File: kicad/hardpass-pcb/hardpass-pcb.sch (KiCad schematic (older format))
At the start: 54 parts, among them P1 Pi_Zero, P2 OLED_I2C, SW1 1, SW10 C/UP, SW11 0/OK, SW12 OK/DN, SW13 SHUTDN, SW2 2, SW3 3, SW4 4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

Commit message: created footprint for sim slot
will use a linkconn sim connector, available from aliexpress using the term 'samsung note n7000 i9000 9003 sim connector'
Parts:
- C? (x14): footprint (none) -> Capacitors_SMD:C_1206
- R? (x2): footprint (none) -> Resistors_SMD:R_1206
- U?: footprint (none) -> Housings_QFP:LQFP-32_7x7mm_Pitch0.8mm
- U?: footprint (none) -> hardpass:CAF99-08153-S132
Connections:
- net +3V3: no longer C?.1, C?.1, C?.2, C?.2, SW?.1, U?.1 (P17), U?.10 (K2), U?.16 (DCIN), U?.21 (EA_N), U?.3 (VDD)
- new net +5V: C?.1, C?.1, C?.2, C?.2, SW?.1, U?.1 (P17), U?.10 (K2), U?.16 (DCIN), U?.21 (EA_N), U?.3 (VDD)
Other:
- note added: "Sim card socket: 'samsung n7000 i9003' style\nhttp://www.linkconn.com/en/product/e08f128a-897a-4361-86f3-81b7a41ba7d4"
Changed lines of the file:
@@
 F 0 "C?" H 10510 3220 50  0000 L CNN
 F 1 "220nF" H 10510 3070 50  0000 L CNN
-F 2 "" H 10500 3150 50  0000 C CNN
+F 2 "Capacitors_SMD:C_1206" H 10600 4850 50  0001 C CNN
 F 3 "" H 10500 3150 50  0000 C CNN
 	1    10500 3150
@@
 F 0 "C?" H 10760 3220 50  0000 L CNN
 F 1 "220nF" H 10760 3070 50  0000 L CNN
-F 2 "" H 10750 3150 50  0000 C CNN
+F 2 "Capacitors_SMD:C_1206" H 10600 4750 50  0001 C CNN
 F 3 "" H 10750 3150 50  0000 C CNN
 	1    10750 3150
@@
 F 0 "C?" H 10110 3870 50  0000 L CNN
 F 1 "100nF" V 10000 3650 50  0000 L CNN
-F 2 "" H 10100 3800 50  0000 C CNN
+F 2 "Capacitors_SMD:C_1206" H 10100 3800 50  0001 C CNN
 F 3 "" H 10100 3800 50  0000 C CNN
 	1    10100 3800
@@
 F 0 "C?" H 10110 4070 50  0000 L CNN
 F 1 "10µF" V 10200 3850 50  0000 L CNN
-F 2 "" H 10100 4000 50  0000 C CNN
+F 2 "Capacitors_SMD:C_1206" H 10100 4000 50  0001 C CNN
 F 3 "" H 10100 4000 50  0000 C CNN
 	1    10100 4000
@@
 F 0 "C?" H 9710 3670 50  0000 L CNN
 F 1 "220nF" H 9710 3520 50  0000 L CNN
-F 2 "" H 9700 3600 50  0000 C CNN
+F 2 "Capacitors_SMD:C_1206" H 9700 3600 50  0001 C CNN
 F 3 "" H 9700 3600 50  0000 C CNN
 	1    9700 3600
@@
 F 0 "C?" H 8360 3670 50  0000 L CNN
 F 1 "100pF" H 8360 3520 50  0000 L CNN
-F 2 "" H 8350 3600 50  0000 C CNN
+F 2 "Capacitors_SMD:C_1206" H 8350 3600 50  0001 C CNN
 F 3 "" H 8350 3600 50  0000 C CNN
 	1    8350 3600
@@
 F 0 "C?" H 7660 3470 50  0000 L CNN
 F 1 "220nF" H 7660 3320 50  0000 L CNN
-F 2 "" H 7650 3400 50  0000 C CNN
+F 2 "Capacitors_SMD:C_1206" H 7650 3400 50  0001 C CNN
 F 3 "" H 7650 3400 50  0000 C CNN
 	1    7650 3400
@@
 F 0 "C?" V 8750 2750 50  0000 L CNN
 F 1 "22nF" V 8750 2450 50  0000 L CNN
-F 2 "" H 8700 2700 50  0000 C CNN
+F 2 "Capacitors_SMD:C_1206" V 7350 4600 50  0001 C CNN
 F 3 "" H 8700 2700 50  0000 C CNN
 	1    8700 2700
@@
 F 0 "C?" H 8460 2270 50  0000 L CNN
 F 1 "100nF" V 8350 2100 50  0000 L CNN
-F 2 "" H 8450 2200 50  0000 C CNN
+F 2 "Capacitors_SMD:C_1206" V 9400 50  50  0001 C CNN
 F 3 "" H 8450 2200 50  0000 C CNN
 	1    8450 2200
@@
 F 0 "C?" H 8460 2020 50  0000 L CNN
 F 1 "10µF" V 8350 1850 50  0000 L CNN
-F 2 "" H 8450 1950 50  0000 C CNN
+F 2 "Capacitors_SMD:C_1206" V 9250 -200 50  0001 C CNN
 F 3 "" H 8450 1950 50  0000 C CNN
 	1    8450 1950
@@
 $EndComp
 $Comp
-L +3V3 #PWR?
-U 1 1 5880FFCE
-P 8600 1950
-F 0 "#PWR?" H 8600 1800 50  0001 C CNN
-F 1 "+3V3" H 8600 2090 50  0001 C CNN
-F 2 "" H 8600 1950 50  0000 C CNN
-F 3 "" H 8600 1950 50  0000 C CNN
-	1    8600 1950
-	1    0    0    -1
-$EndComp
-$Comp
-L +3V3 #PWR?
-U 1 1 588135B2
-P 10650 2500
-F 0 "#PWR?" H 10650 2350 50  0001 C CNN
-F 1 "+3V3" H 10650 2640 50  0000 C CNN
-F 2 "" H 10650 2500 50  0000 C CNN
-F 3 "" H 10650 2500 50  0000 C CNN
-	1    10650 2500
-	1    0    0    -1
-$EndComp
-$Comp
 L GND #PWR?
 U 1 1 5881377E
@@
 F 0 "U?" H 7050 3550 60  0000 C CNN
 F 1 "ISO7816" H 7050 2750 60  0000 C CNN
-F 2 "" H 7050 3250 60  0001 C CNN
+F 2 "hardpass:CAF99-08153-S132" H 7050 3250 60  0001 C CNN
 F 3 "" H 7050 3250 60  0001 C CNN
 	1    7050 3150
 	1    0    0    1
-$EndComp
-$Comp
-L +3V3 #PWR?
-U 1 1 58821E3C
-P 7550 2900
-F 0 "#PWR?" H 7550 2750 50  0001 C CNN
-F 1 "+3V3" H 7550 3040 50  0001 C CNN
-F 2 "" H 7550 2900 50  0000 C CNN
-F 3 "" H 7550 2900 50  0000 C CNN
-	1    7550 2900
-	1    0    0    -1
 $EndComp
 NoConn ~ 7450 3100
@@
 F 0 "R?" H 8230 2820 50  0000 L CNN
 F 1 "180" H 8230 2760 50  0000 L CNN
-F 2 "" H 8200 2800 50  0000 C CNN
+F 2 "Resistors_SMD:R_1206" H 8200 2800 50  0001 C CNN
 F 3 "" H 8200 2800 50  0000 C CNN
 	1    8200 2800
@@
 F 0 "C?" H 8060 3270 50  0000 L CNN
 F 1 "33pF" H 8060 3120 50  0000 L CNN
-F 2 "" H 8050 3200 50  0000 C CNN
+F 2 "Capacitors_SMD:C_1206" H 8050 3200 50  0001 C CNN
 F 3 "" H 8050 3200 50  0000 C CNN
 	1    8050 3200
@@
 F 0 "C?" H 8860 3670 50  0000 L CNN
 F 1 "100pF" H 8860 3520 50  0000 L CNN
-F 2 "" H 8850 3600 50  0000 C CNN
+F 2 "Capacitors_SMD:C_1206" H 8850 3600 50  0001 C CNN
 F 3 "" H 8850 3600 50  0000 C CNN
 	1    8850 3600
@@
 	1    0    0    -1
 $EndComp
-$Comp
-L +3V3 #PWR?
-U 1 1 58833391
-P 10200 3400
-F 0 "#PWR?" H 10200 3250 50  0001 C CNN
-F 1 "+3V3" H 10200 3540 50  0000 C CNN
-F 2 "" H 10200 3400 50  0000 C CNN
-F 3 "" H 10200 3400 50  0000 C CNN
-	1    10200 3400
-	1    0    0    -1
-$EndComp
 Text Notes 6450 4300 0    60   ~ 0
 http://www.nxp.com/documents/application_note/AN10207.pdf\nhttp://www.nxp.com/documents/data_sheet/TDA8029.pdf
@@
 F 0 "C?" H 10010 1270 50  0000 L CNN
 F 1 "22pF" H 10010 1120 50  0000 L CNN
-F 2 "" H 10000 1200 50  0000 C CNN
+F 2 "Capacitors_SMD:C_1206" H 10600 1350 50  0001 C CNN
 F 3 "" H 10000 1200 50  0000 C CNN
 	1    10000 1200
@@
 F 0 "C?" H 9710 1270 50  0000 L CNN
 F 1 "22pF" H 9710 1120 50  0000 L CNN
-F 2 "" H 9700 1200 50  0000 C CNN
+F 2 "Capacitors_SMD:C_1206" H 8800 1450 50  0001 C CNN
 F 3 "" H 9700 1200 50  0000 C CNN
 	1    9700 1200
@@
 $EndComp
 $Comp
-L +3V3 #PWR?
-U 1 1 58840082
-P 9500 1500
-F 0 "#PWR?" H 9500 1350 50  0001 C CNN
-F 1 "+3V3" H 9500 1640 50  0001 C CNN
-F 2 "" H 9500 1500 50  0000 C CNN
-F 3 "" H 9500 1500 50  0000 C CNN
-	1    9500 1500
-	1    0    0    -1
-$EndComp
-$Comp
-L +3V3 #PWR?
-U 1 1 58843822
-P 8800 2200
-F 0 "#PWR?" H 8800 2050 50  0001 C CNN
-F 1 "+3V3" H 8800 2340 50  0001 C CNN
-F 2 "" H 8800 2200 50  0000 C CNN
-F 3 "" H 8800 2200 50  0000 C CNN
-	1    8800 2200
-	1    0    0    -1
-$EndComp
-$Comp
 L TDA8029 U?
 U 1 1 5880AAA0
@@
 F 0 "U?" H 9650 2450 60  0000 C CNN
 F 1 "TDA8029" H 9650 2650 60  0000 C CNN
-F 2 "" H 9650 2550 60  0001 C CNN
+F 2 "Housings_QFP:LQFP-32_7x7mm_Pitch0.8mm" H 9650 2550 60  0001 C CNN
 F 3 "" H 9650 2550 60  0001 C CNN
 	1    9650 2550
@@
 Wire Wire Line
 	7450 2900 7550 2900
-Wire Notes Line
-	8250 3500 8250 3700
-Wire Notes Line
-	8250 3700 8450 3700
-Wire Notes Line
-	8450 3700 8450 3500
-Wire Notes Line
-	8450 3500 8250 3500
 $Comp
 L R_Small R?
@@
 F 0 "R?" H 7730 3220 50  0000 L CNN
 F 1 "100" H 7730 3160 50  0000 L CNN
-F 2 "" H 7700 3200 50  0000 C CNN
+F 2 "Resistors_SMD:R_1206" H 7700 3200 50  0001 C CNN
 F 3 "" H 7700 3200 50  0000 C CNN
 	1    7700 3200
@@
 	7950 3200 7800 3200
 Wire Notes Line
-	8750 3500 8750 3700
-Wire Notes Line
-	8750 3700 8950 3700
-Wire Notes Line
-	8950 3700 8950 3500
-Wire Notes Line
-	8950 3500 8750 3500
-Wire Notes Line
-	8000 3300 8100 3300
-Wire Notes Line
-	8100 3300 8100 3100
-Wire Notes Line
-	8100 3100 8000 3100
-Wire Notes Line
-	8000 3100 8000 3300
-Wire Notes Line
-	7600 3250 7600 3500
-Wire Notes Line
-	7600 3500 7700 3500
-Wire Notes Line
-	7700 3500 7700 3250
-Wire Notes Line
-	7700 3250 7600 3250
-Wire Notes Line
 	6150 650  6150 4550
 Wire Notes Line
@@
 Text Notes 6400 1300 0    60   ~ 0
 possible driver:\nhttps://github.com/larytet/TDA8029
+$Comp
+L +5V #PWR?
+U 1 1 588108E7
+P 8600 1950
+F 0 "#PWR?" H 8600 1800 50  0001 C CNN
+F 1 "+5V" H 8600 2090 50  0000 C CNN
+F 2 "" H 8600 1950 50  0000 C CNN
+F 3 "" H 8600 1950 50  0000 C CNN
+	1    8600 1950
+	1    0    0    -1
+$EndComp
+$Comp
+L +5V #PWR?
+U 1 1 58810991
+P 8800 2200
+F 0 "#PWR?" H 8800 2050 50  0001 C CNN
+F 1 "+5V" H 8800 2340 50  0000 C CNN
+F 2 "" H 8800 2200 50  0000 C CNN
+F 3 "" H 8800 2200 50  0000 C CNN
+	1    8800 2200
+	1    0    0    -1
+$EndComp
+$Comp
+L +5V #PWR?
+U 1 1 58810A71
+P 10650 2500
+F 0 "#PWR?" H 10650 2350 50  0001 C CNN
+F 1 "+5V" H 10650 2640 50  0000 C CNN
+F 2 "" H 10650 2500 50  0000 C CNN
+F 3 "" H 10650 2500 50  0000 C CNN
+	1    10650 2500
+	1    0    0    -1
+$EndComp
+$Comp
+L +5V #PWR?
+U 1 1 58810B51
+P 10200 3400
+F 0 "#PWR?" H 10200 3250 50  0001 C CNN
+F 1 "+5V" H 10200 3540 50  0000 C CNN
+F 2 "" H 10200 3400 50  0000 C CNN
+F 3 "" H 10200 3400 50  0000 C CNN
+	1    10200 3400
+	1    0    0    -1
+$EndComp
+$Comp
+L +5V #PWR?
+U 1 1 588110F4
+P 9500 1500
+F 0 "#PWR?" H 9500 1350 50  0001 C CNN
+F 1 "+5V" H 9500 1640 50  0000 C CNN
+F 2 "" H 9500 1500 50  0000 C CNN
+F 3 "" H 9500 1500 50  0000 C CNN
+	1    9500 1500
+	1    0    0    -1
+$EndComp
+$Comp
+L +5V #PWR?
+U 1 1 588119E7
+P 7550 2900
+F 0 "#PWR?" H 7550 2750 50  0001 C CNN
+F 1 "+5V" H 7550 3040 50  0000 C CNN
+F 2 "" H 7550 2900 50  0000 C CNN
+F 3 "" H 7550 2900 50  0000 C CNN
+	1    7550 2900
+	1    0    0    -1
+$EndComp
+Text Notes 6450 4500 0    60   ~ 0
+Sim card socket: 'samsung n7000 i9003' style\nhttp://www.linkconn.com/en/product/e08f128a-897a-4361-86f3-81b7a41ba7d4
 $EndSCHEMATC

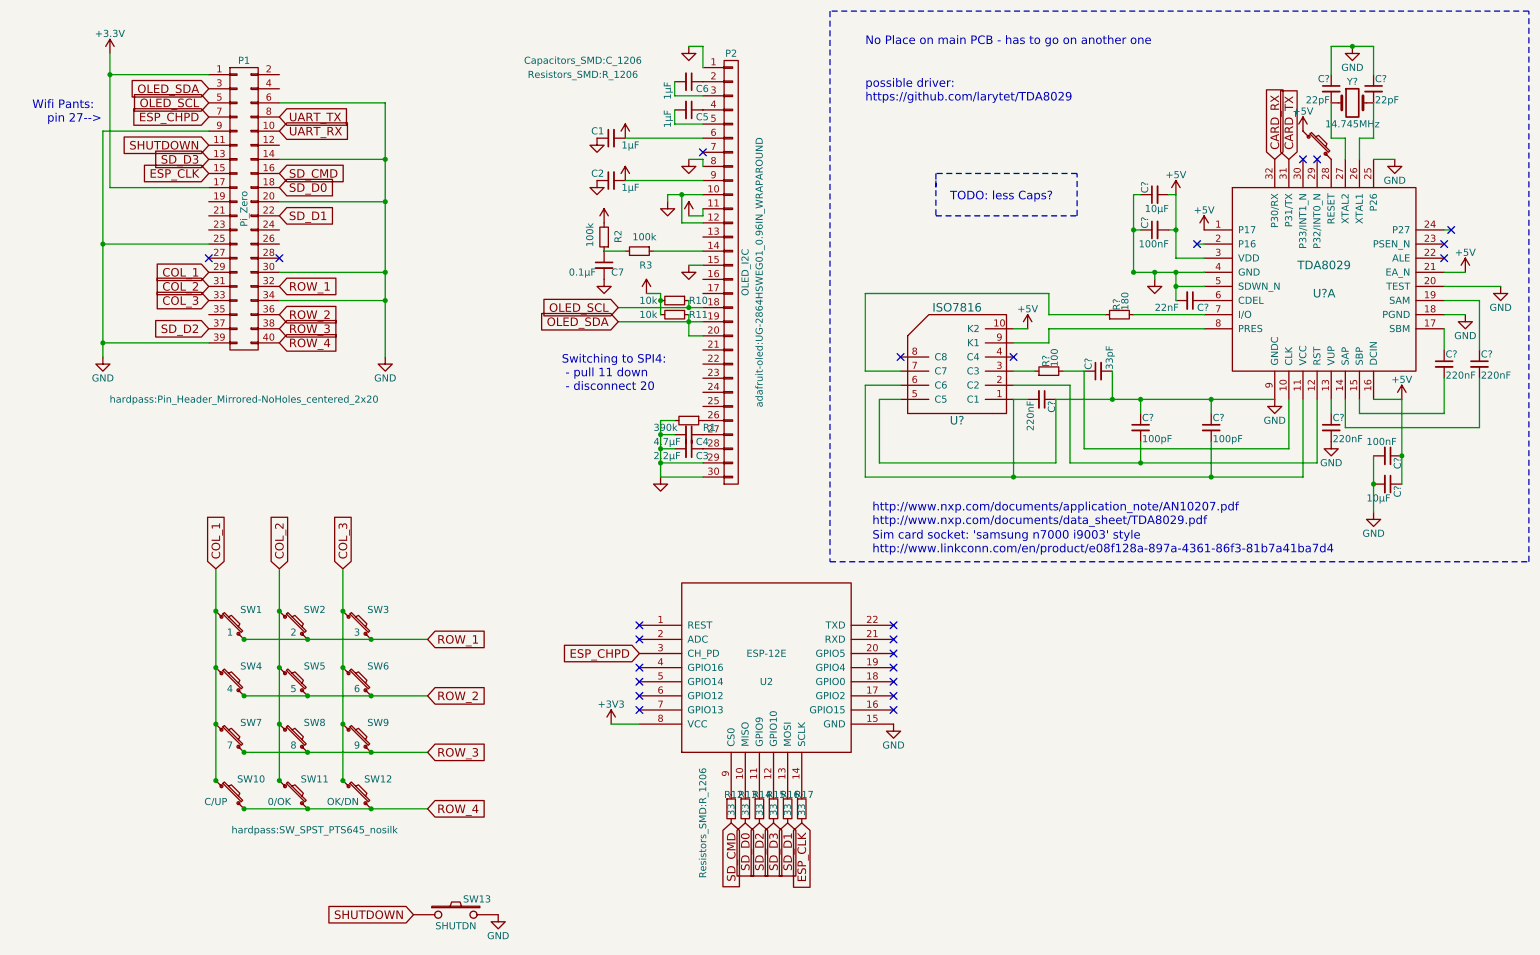
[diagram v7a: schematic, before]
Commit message: added pin header for second board
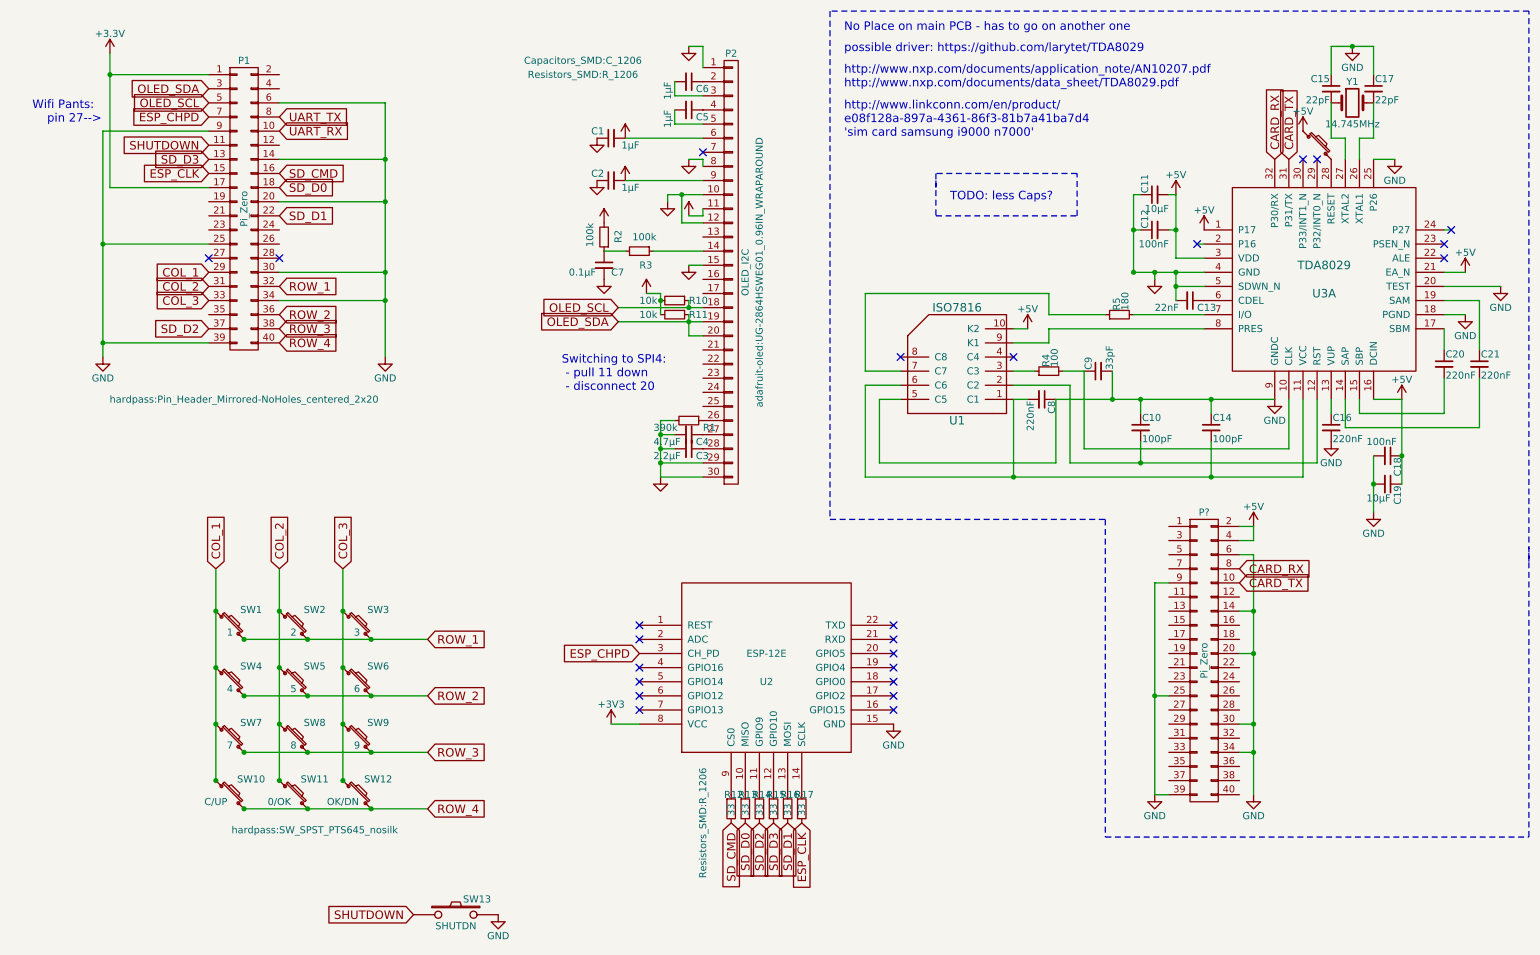
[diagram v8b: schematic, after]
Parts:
- added P?: Pi_Zero, Pin_Headers:Pin_Header_Straight_2x20_Pitch2.54mm, symbol CONN_02X20
- gave numbers to parts that had none: 20
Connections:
- net +5V: now also P?.2 (P2), P?.4 (P4)
- net CARD_RX: now also P?.8 (P8)
- net CARD_TX: now also P?.10 (P10)
- net GND: now also P?.14 (P14), P?.20 (P20), P?.25 (P25), P?.30 (P30), P?.34 (P34), P?.39 (P39), P?.6 (P6), P?.9 (P9)
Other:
- note added: "http://www.linkconn.com/en/product/\ne08f128a-897a-4361-86f3-81b7a41ba7d4\n'sim card samsung i9000 n7000'"
- note added: "possible driver: https://github.com/larytet/TDA8029"
- note removed: "Sim card socket: 'samsung n7000 i9003' style\nhttp://www.linkconn.com/en/product/e08f128a-897a-4361-86f3-81b7a41ba7d4"
- note removed: "possible driver:\nhttps://github.com/larytet/TDA8029"
